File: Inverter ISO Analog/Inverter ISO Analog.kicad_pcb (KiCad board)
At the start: 2 copper layers, 27.8 x 58.4 mm, 6 parts, among them J1 Inverter, J2 Brake Sensor, J3 Motor, J4 Accelerator Sensor, U1 C2000BoosterPack_Shield

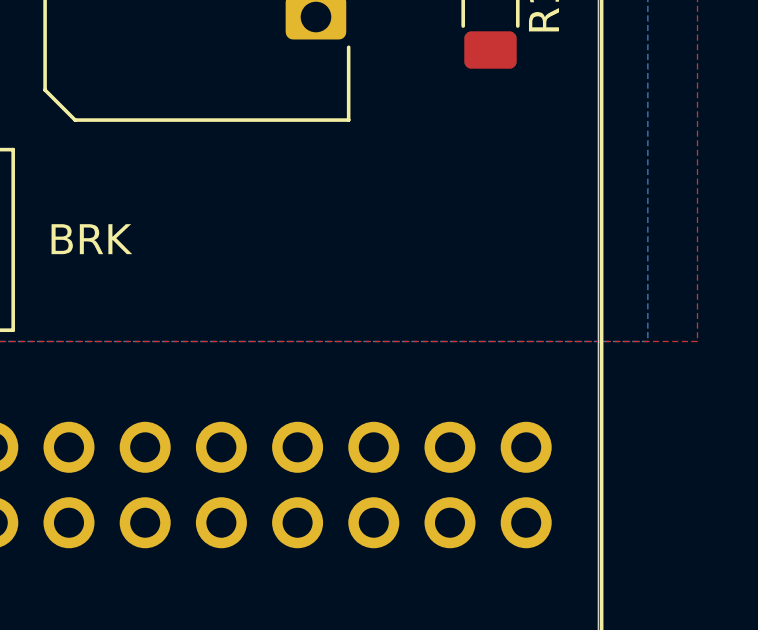
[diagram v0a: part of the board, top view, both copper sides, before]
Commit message: Vibration damping fasteners added to all PCB shields
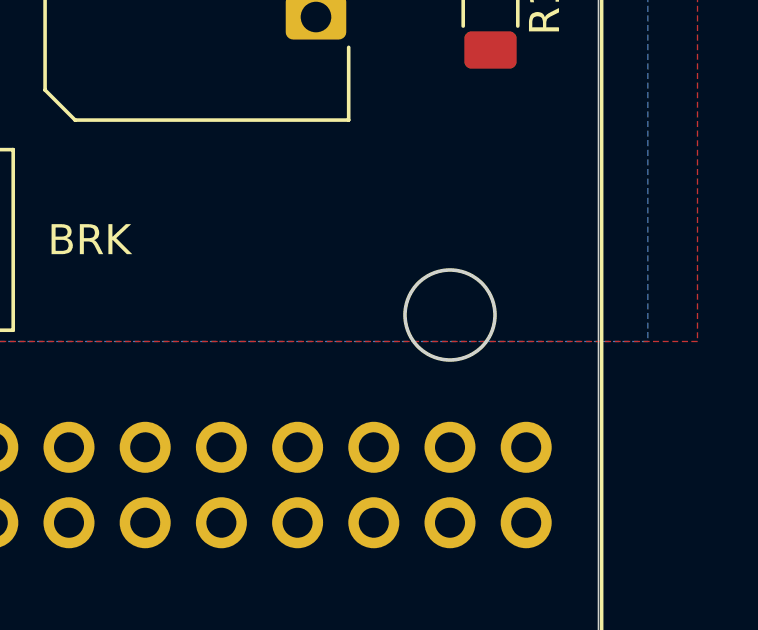
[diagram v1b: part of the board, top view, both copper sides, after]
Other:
- outline, holes or cut-outs redrawn
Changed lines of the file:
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@@
   (general
     (thickness 1.6)
-    (drawings 8)
+    (drawings 9)
     (tracks 20)
     (zones 0)
@@
     (solder_mask_min_width 0.25)
     (aux_axis_origin 0 0)
-    (visible_elements FFFFFF7F)
+    (visible_elements 7FFFFFFF)
     (pcbplotparams
       (layerselection 0x010fc_ffffffff)
@@
     )
   )
+  (gr_circle (center 153.051821 116.526061) (end 154.551821 116.526061) (layer Edge.Cuts) (width 0.12))
   (gr_text Inverter (at 137.7823 100.18522 90) (layer F.SilkS)
     (effects (font (size 1 1) (thickness 0.15)))
